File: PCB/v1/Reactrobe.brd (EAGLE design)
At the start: 59.9 x 15.9 mm, 26 parts, among them J1 OSTVN02A150, J2 OSTVN03A150, U1 ATMEGA328P-AU, U2 NCP1117ST50T3G, U3 MAX9814, Y1 FA-238 16.0000MB-C3

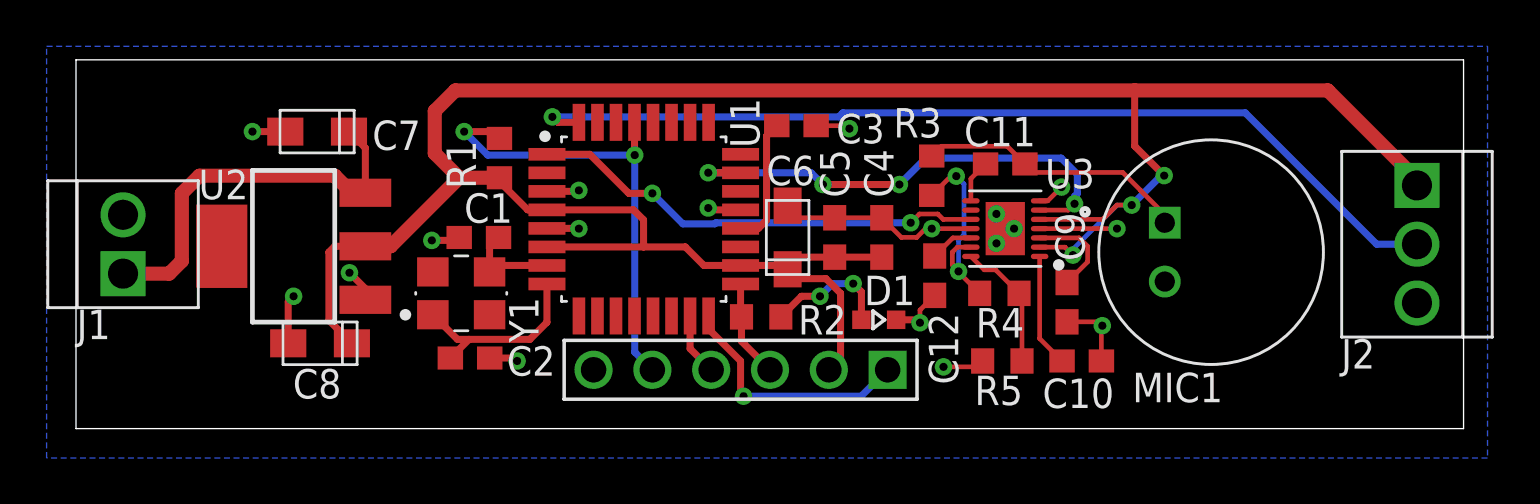
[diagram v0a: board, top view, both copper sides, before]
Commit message: PCB mods, added first untested case.
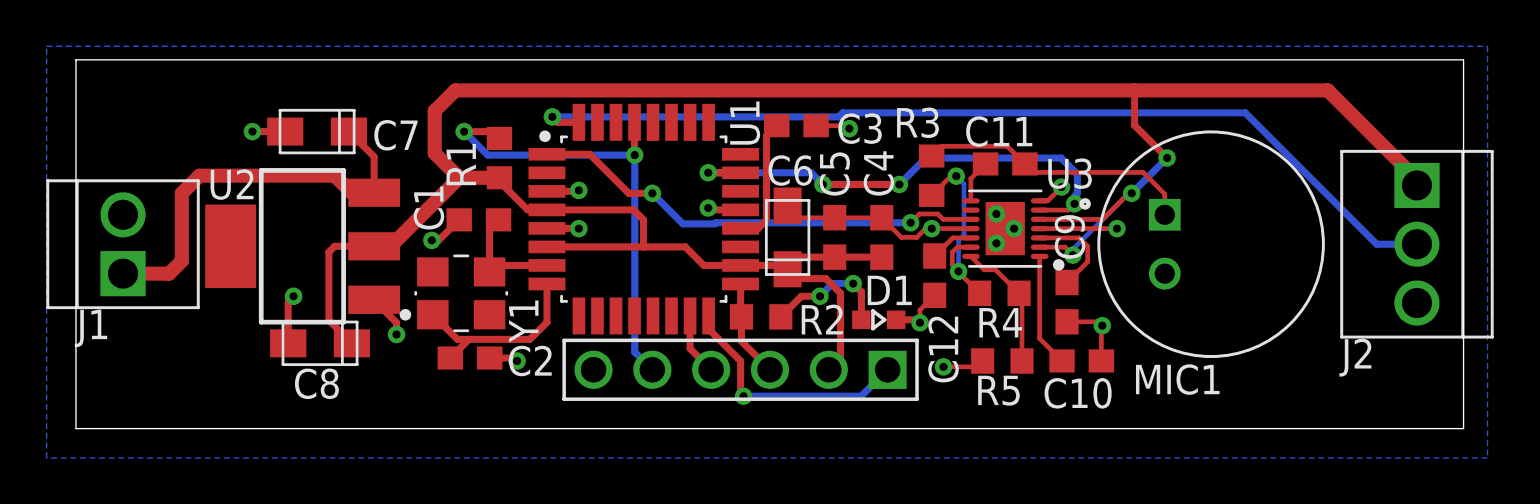
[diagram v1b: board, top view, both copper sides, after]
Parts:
- moved C1 0.76 mm to (17.4, 9.02)
- moved U2 0.38 mm to (9.78, 7.87)
- moved MIC1 0.34 mm to (49.0, 7.96)
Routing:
- net N$2: track 4.24 -> 5.00 mm
- net GND: track 33.8 -> 34.5 mm
- net VIN: track 17.2 -> 17.7 mm
